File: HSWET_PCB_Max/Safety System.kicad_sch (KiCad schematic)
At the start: 7 parts, among them U4 LTC3525ESC6-5-TRMPBF, U5 SN74HC14N

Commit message: pushing one added cap
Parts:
- added C4: 0.47, footprints:CAPPRD500W60D1000H3150, symbol Device:C
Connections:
- net GND: now also C4.2
- net at C2.1, L1.1, R9.2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: now also C4.1
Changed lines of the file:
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@@
+	)
+	(junction
+		(at 125.73 59.69)
+		(diameter 0)
+		(color 0 0 0 0)
 	)
 	(junction
@@
 	(wire
 		(pts
-			(xy 121.92 59.69) (xy 130.81 59.69)
+			(xy 121.92 59.69) (xy 125.73 59.69)
+		)
+		(stroke
+			(width 0)
+			(type default)
+		)
+	)
+	(wire
+		(pts
+			(xy 125.73 59.69) (xy 130.81 59.69)
 		)
 		(stroke
@@
 	)
 	(symbol
+		(lib_id "Device:C")
+		(at 125.73 63.5 0)
+		(unit 1)
+		(exclude_from_sim no)
+		(in_bom yes)
+		(on_board yes)
+		(dnp no)
+		(property "Reference" "C4"
+			(at 119.888 64.008 0)
+			(effects
+				(font
+					(size 1.27 1.27)
+				)
+				(justify left)
+			)
+		)
+		(property "Value" "0.47"
+			(at 119.888 66.548 0)
+			(effects
+				(font
+					(size 1.27 1.27)
+				)
+				(justify left)
+			)
+		)
+		(property "Footprint" "footprints:CAPPRD500W60D1000H3150"
+			(at 126.6952 67.31 0)
+			(effects
+				(font
+					(size 1.27 1.27)
+				)
+				(hide yes)
+			)
+		)
+		(property "Datasheet" "~"
+			(at 125.73 63.5 0)
+			(effects
+				(font
+					(size 1.27 1.27)
+				)
+				(hide yes)
+			)
+		)
+		(property "Description" "Unpolarized capacitor"
+			(at 125.73 63.5 0)
+			(effects
+				(font
+					(size 1.27 1.27)
+				)
+				(hide yes)
+			)
+		)
+		(pin "2"
+		)
+		(pin "1"
+		)
+		(instances
+			(project "HSWET_PCB"
+				(path "/82d46295-621f-4df3-b604-ae215ede48d5/501fd5c5-e451-49c3-8c4f-86c31ee3b7e4"
+					(reference "C4")
+					(unit 1)
+				)
+			)
+		)
+	)
+	(symbol
 		(lib_id "Safety System Library:LTC3525ESC6-5-TRMPBF")
 		(at 135.89 54.61 0)
@@
 					(unit 1)
 				)
+			)
+		)
+	)
+	(symbol
+		(lib_id "power:GND")
+		(at 125.73 67.31 0)
+		(unit 1)
+		(exclude_from_sim no)
+		(in_bom yes)
+		(on_board yes)
+		(dnp no)
+		(fields_autoplaced yes)
+		(property "Reference" "#PWR022"
+			(at 125.73 73.66 0)
+			(effects
+				(font
+					(size 1.27 1.27)
+				)
+				(hide yes)
+			)
+		)
+		(property "Value" "GND"
+			(at 125.73 72.39 0)
+			(effects
+				(font
+					(size 1.27 1.27)
+				)
+			)
+		)
+		(property "Footprint" ""
+			(at 125.73 67.31 0)
+			(effects
+				(font
+					(size 1.27 1.27)
+				)
+				(hide yes)
+			)
+		)
+		(property "Datasheet" ""
+			(at 125.73 67.31 0)
+			(effects
+				(font
+					(size 1.27 1.27)
+				)
+				(hide yes)
+			)
+		)
+		(property "Description" "Power symbol creates a global label with name \"GND\" , ground"
+			(at 125.73 67.31 0)
+			(effects
+				(font
+					(size 1.27 1.27)
+				)
+				(hide yes)
+			)
+		)
+		(pin "1"
+		)
+		(instances
+			(project ""
+				(path "/82d46295-621f-4df3-b604-ae215ede48d5/501fd5c5-e451-49c3-8c4f-86c31ee3b7e4"
+					(reference "#PWR022")
+					(unit 1)
+				)

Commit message: swithced resistor and diode
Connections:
- net 5V_BUCK: now also R9.1; no longer D1.2 (A)
- net at C2.1, C4.1, L1.1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: now also D1.1 (K); no longer R9.2
- new net: D1.2 (A), R9.2
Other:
- moved on the sheet: D1, R9
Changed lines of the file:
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@@
+	)
+	(junction
+		(at 190.5 59.69)
+		(diameter 0)
+		(color 0 0 0 0)
+	)
+	(junction
+		(at 130.81 59.69)
+		(diameter 0)
+		(color 0 0 0 0)
+	)
+	(junction
+		(at 134.62 59.69)
+		(diameter 0)
+		(color 0 0 0 0)
+	)
+	(junction
+		(at 107.95 59.69)
+		(diameter 0)
+		(color 0 0 0 0)
 	)
 	(junction
@@
 	)
 	(junction
-		(at 190.5 59.69)
-		(diameter 0)
-		(color 0 0 0 0)
-	)
-	(junction
-		(at 107.95 59.69)
-		(diameter 0)
-		(color 0 0 0 0)
-	)
-	(junction
-		(at 130.81 59.69)
-		(diameter 0)
-		(color 0 0 0 0)
-	)
-	(junction
-		(at 134.62 59.69)
-		(diameter 0)
-		(color 0 0 0 0)
-	)
-	(junction
 		(at 179.07 59.69)
 		(diameter 0)
@@
 	(wire
 		(pts
+			(xy 107.95 59.69) (xy 109.22 59.69)
+		)
+		(stroke
+			(width 0)
+			(type default)
+		)
+	)
+	(wire
+		(pts
 			(xy 106.68 59.69) (xy 107.95 59.69)
 		)
@@
 	(wire
 		(pts
+			(xy 114.3 59.69) (xy 115.57 59.69)
+		)
+		(stroke
+			(width 0)
+			(type default)
+		)
+	)
+	(wire
+		(pts
 			(xy 107.95 59.69) (xy 107.95 87.63)
 		)
@@
 	(wire
 		(pts
-			(xy 121.92 59.69) (xy 125.73 59.69)
-		)
-		(stroke
-			(width 0)
-			(type default)
-		)
-	)
-	(wire
-		(pts
 			(xy 125.73 59.69) (xy 130.81 59.69)
 		)
@@
 	(wire
 		(pts
+			(xy 123.19 59.69) (xy 125.73 59.69)
+		)
+		(stroke
+			(width 0)
+			(type default)
+		)
+	)
+	(wire
+		(pts
 			(xy 134.62 72.39) (xy 152.4 72.39)
 		)
@@
 		(pts
 			(xy 179.07 59.69) (xy 190.5 59.69)
-		)
-		(stroke
-			(width 0)
-			(type default)
-		)
-	)
-	(wire
-		(pts
-			(xy 115.57 59.69) (xy 116.84 59.69)
 		)
 		(stroke
@@
 	(symbol
 		(lib_id "Diode:1N4148WT")
-		(at 111.76 59.69 180)
+		(at 119.38 59.69 180)
 		(unit 1)
 		(exclude_from_sim no)
@@
 		(fields_autoplaced yes)
 		(property "Reference" "D1"
-			(at 111.76 53.34 0)
+			(at 119.38 53.34 0)
 			(effects
 				(font
@@
 		)
 		(property "Value" "STPS120M"
-			(at 111.76 55.88 0)
+			(at 119.38 55.88 0)
 			(effects
 				(font
@@
 		)
 		(property "Footprint" "footprints:DIO_STPS1L40M"
-			(at 111.76 55.245 0)
+			(at 119.38 55.245 0)
 			(effects
 				(font
@@
 		)
 		(property "Datasheet" "https://www.st.com/content/ccc/resource/technical/document/datasheet/9c/58/21/f3/e7/b8/4a/bb/CD00002871.pdf/files/CD00002871.pdf/jcr:content/translations/en.CD00002871.pdf"
-			(at 111.76 59.69 0)
+			(at 119.38 59.69 0)
 			(effects
 				(font
@@
 		)
 		(property "Description" "DIODE SCHOTTKY 20V 1A STMITE"
-			(at 111.76 59.69 0)
+			(at 119.38 59.69 0)
 			(effects
 				(font
@@
 		)
 		(property "Sim.Device" "D"
-			(at 111.76 59.69 0)
+			(at 119.38 59.69 0)
 			(effects
 				(font
@@
 		)
 		(property "Sim.Pins" "1=K 2=A"
-			(at 111.76 59.69 0)
+			(at 119.38 59.69 0)
 			(effects
 				(font
@@
 	(symbol
 		(lib_id "Device:R_Small_US")
-		(at 119.38 59.69 90)
+		(at 111.76 59.69 90)
 		(unit 1)
 		(exclude_from_sim no)
@@
 		(dnp no)
 		(property "Reference" "R9"
-			(at 117.856 62.484 90)
+			(at 110.236 62.484 90)
 			(effects
 				(font
@@
 		)
 		(property "Value" "10"
-			(at 117.856 65.024 90)
+			(at 110.236 65.024 90)
 			(effects
 				(font
@@
 		)
 		(property "Footprint" "Resistor_SMD:R_2512_6332Metric"
-			(at 119.38 59.69 0)
+			(at 111.76 59.69 0)
 			(effects
 				(font
@@
 		)
 		(property "Datasheet" "~"
-			(at 119.38 59.69 0)
+			(at 111.76 59.69 0)
 			(effects
 				(font
@@
 		)
 		(property "Description" "Resistor, small US symbol"
-			(at 119.38 59.69 0)
-			(effects
-				(font
+			(at 111.76 59.69 0)
+			(effects
+				(font

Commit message: added maybe unecessary plane, swapped 1x05 connector -> 1x04 after mirabel got rid of 6v, ficed footprint for lm2596
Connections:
- net 5V_BUCK renamed 4.5V_BUCK
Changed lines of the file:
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@@
 		)
 	)
-	(global_label "5V_BUCK"
+	(global_label "4.5V_BUCK"
 		(shape input)
 		(at 106.68 59.69 180)
@@
 		)
 		(property "Intersheetrefs" "${INTERSHEET_REFS}"
-			(at 95.2886 59.69 0)
+			(at 93.4743 59.69 0)
 			(effects
 				(font

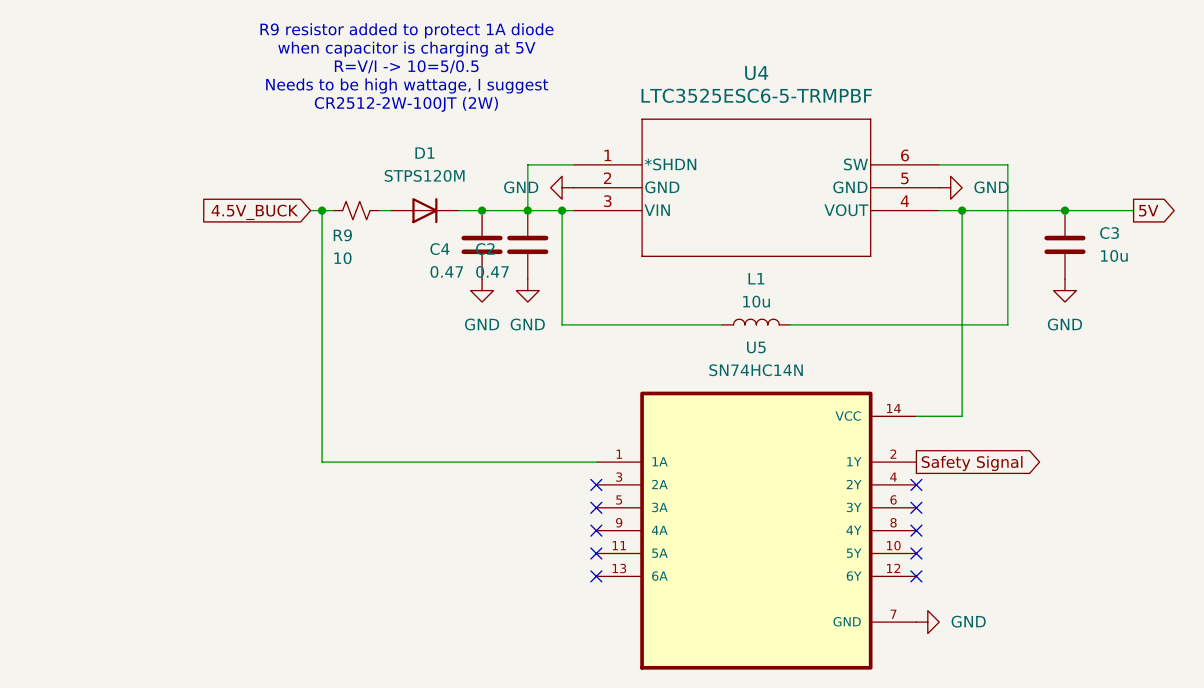
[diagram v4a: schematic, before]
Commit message: labelled everything, cleanup up various things, corrected inductor, removed schmitt
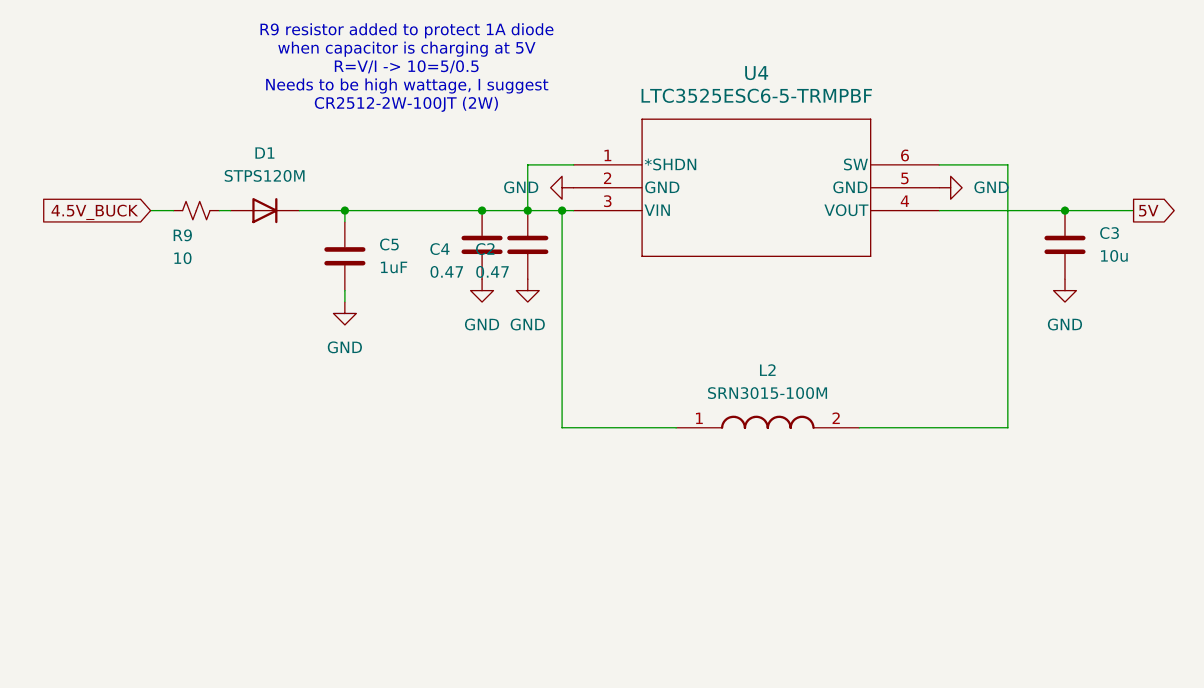
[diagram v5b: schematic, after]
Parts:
- removed L1: 10u, Inductor_SMD:L_0603_1608Metric, symbol Device:L
- removed U5: SN74HC14N, footprints:D14, symbol Safety System Library:SN74HC14N
- added C5: 1uF, Capacitor_SMD:C_0603_1608Metric, symbol Device:C
- added L2: SRN3015-100M, SRN3015, symbol inductor:SRN3015-100M
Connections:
- net GND: now also C5.2
- net at C2.1, C4.1, D1.1 (K)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: now also C5.1, L2.1
- net at U4.6 (SW): now also L2.2
- no-connect marks 10 -> 0
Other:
- moved on the sheet: D1, R9

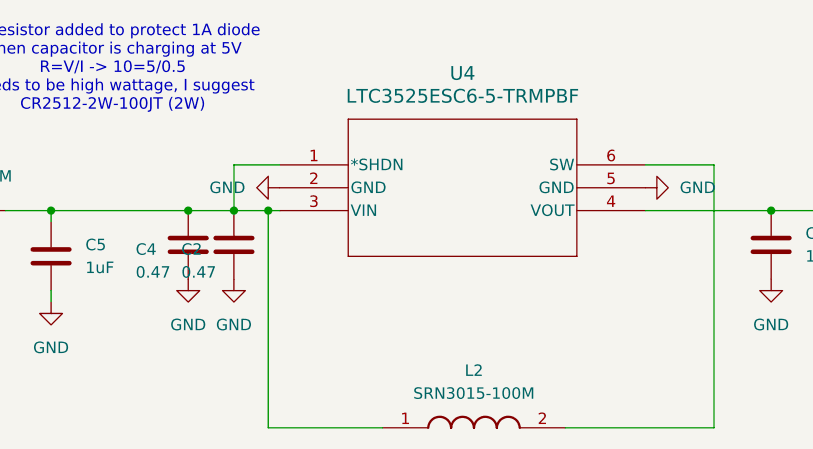
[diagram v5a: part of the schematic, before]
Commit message: fixed lin act schematci
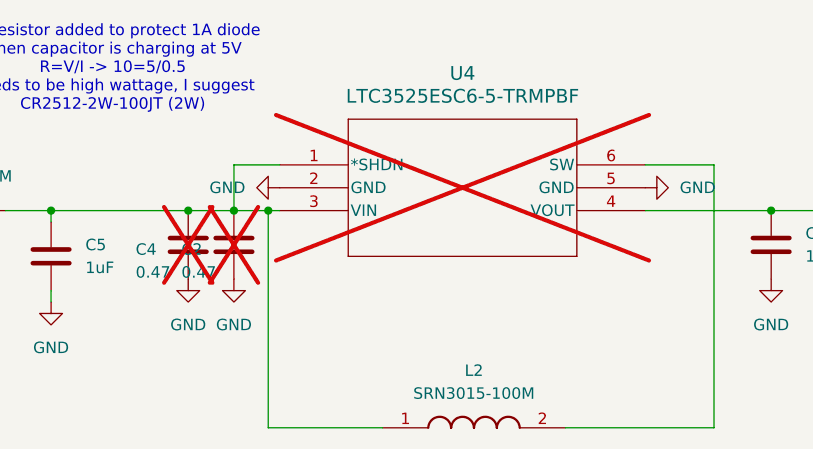
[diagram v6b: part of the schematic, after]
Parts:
- C2, C4, U4: now not fitted
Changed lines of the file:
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@@
 		(in_bom yes)
 		(on_board yes)
-		(dnp no)
+		(dnp yes)
 		(property "Reference" "C4"
 			(at 119.888 64.008 0)
@@
 		(in_bom yes)
 		(on_board yes)
-		(dnp no)
+		(dnp yes)
 		(fields_autoplaced yes)
 		(property "Reference" "U4"
@@
 		(in_bom yes)
 		(on_board yes)
-		(dnp no)
+		(dnp yes)
 		(property "Reference" "C2"
 			(at 124.968 64.008 0)
